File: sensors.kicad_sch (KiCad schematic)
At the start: 13 parts, among them U3 BMP581, U4 BNO085, Y2 Crystal

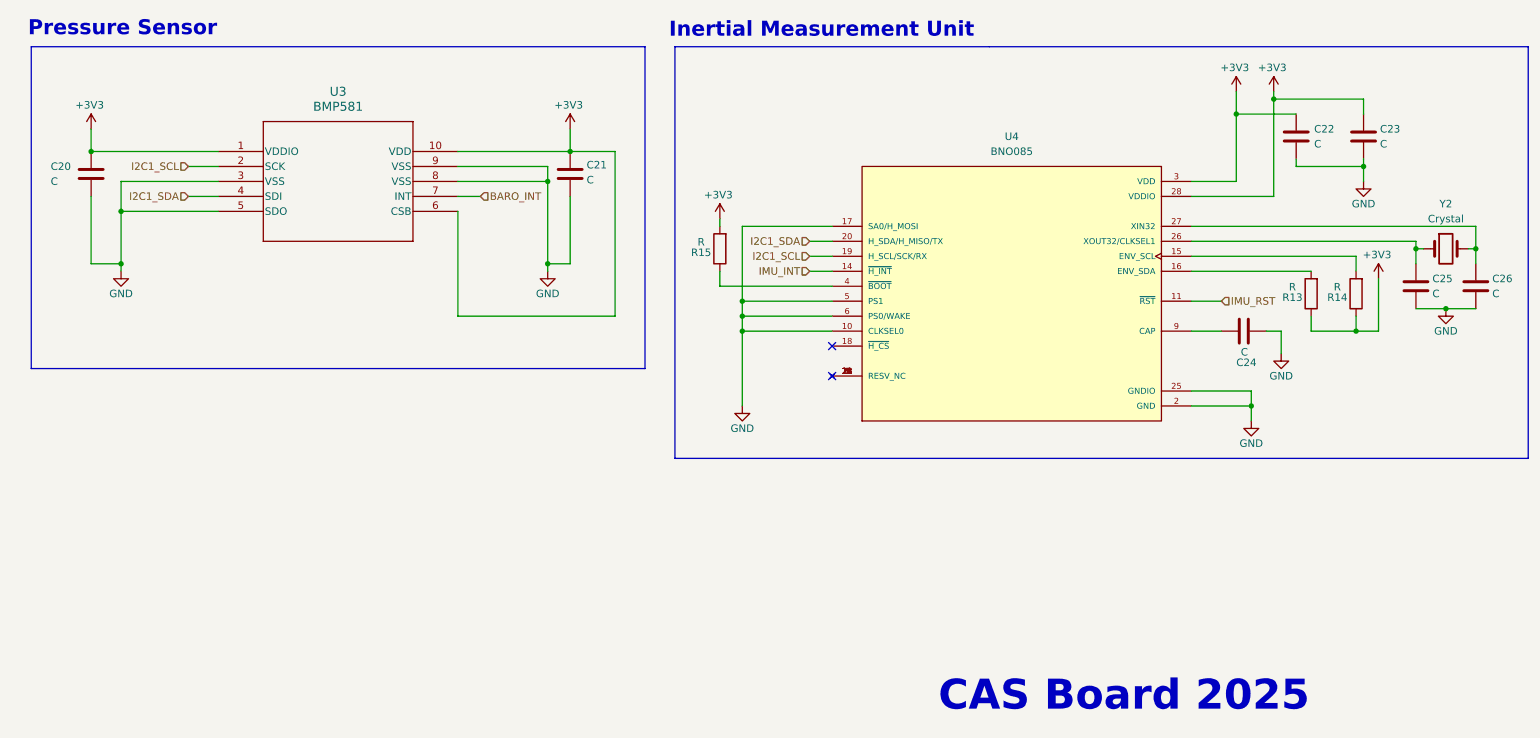
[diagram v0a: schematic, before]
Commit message: Initial layout for PCB components, updated README with images. Removed some test points and headers from final layout. Pending addition of buzzer. Pending additional power testing and pending routing.
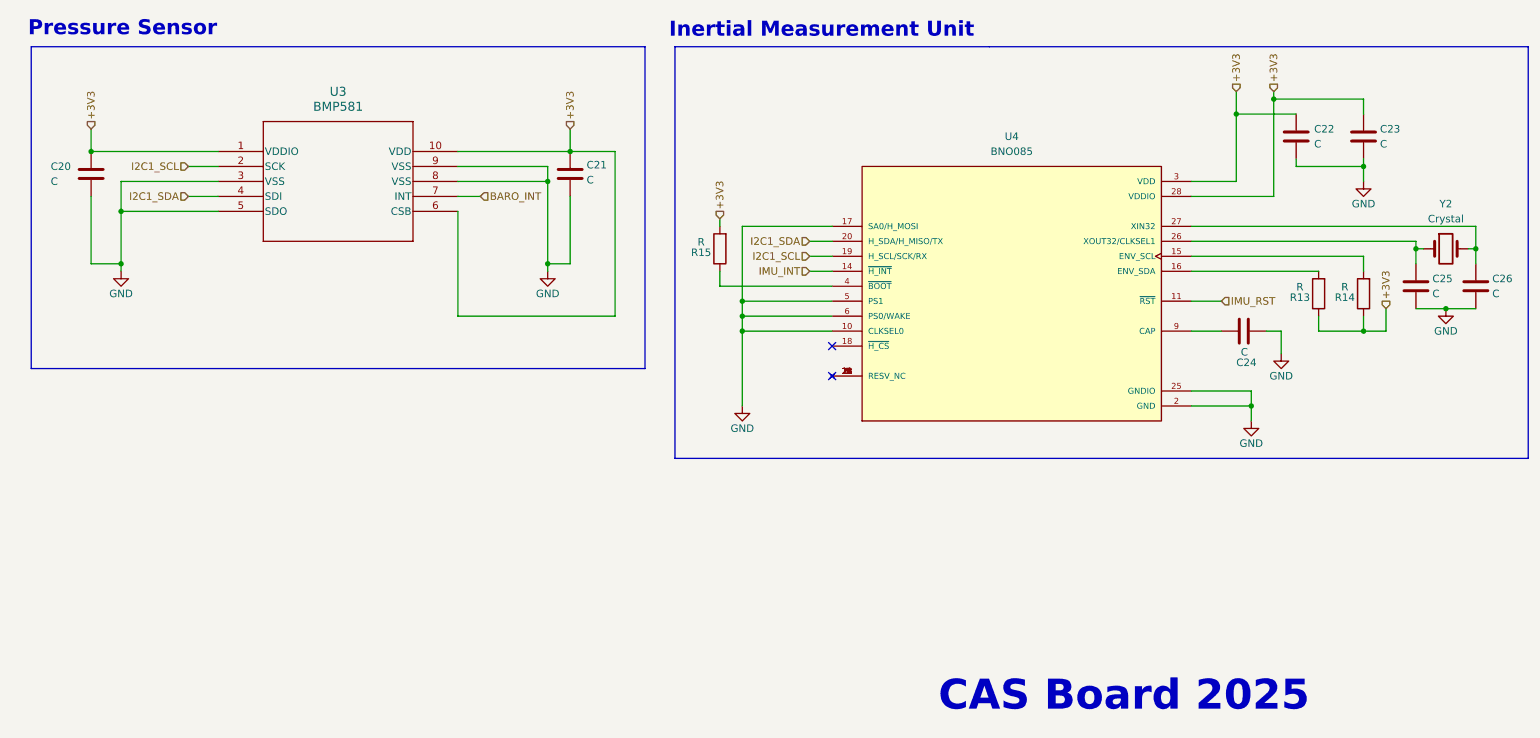
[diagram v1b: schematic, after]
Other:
- moved on the sheet: R13, R14

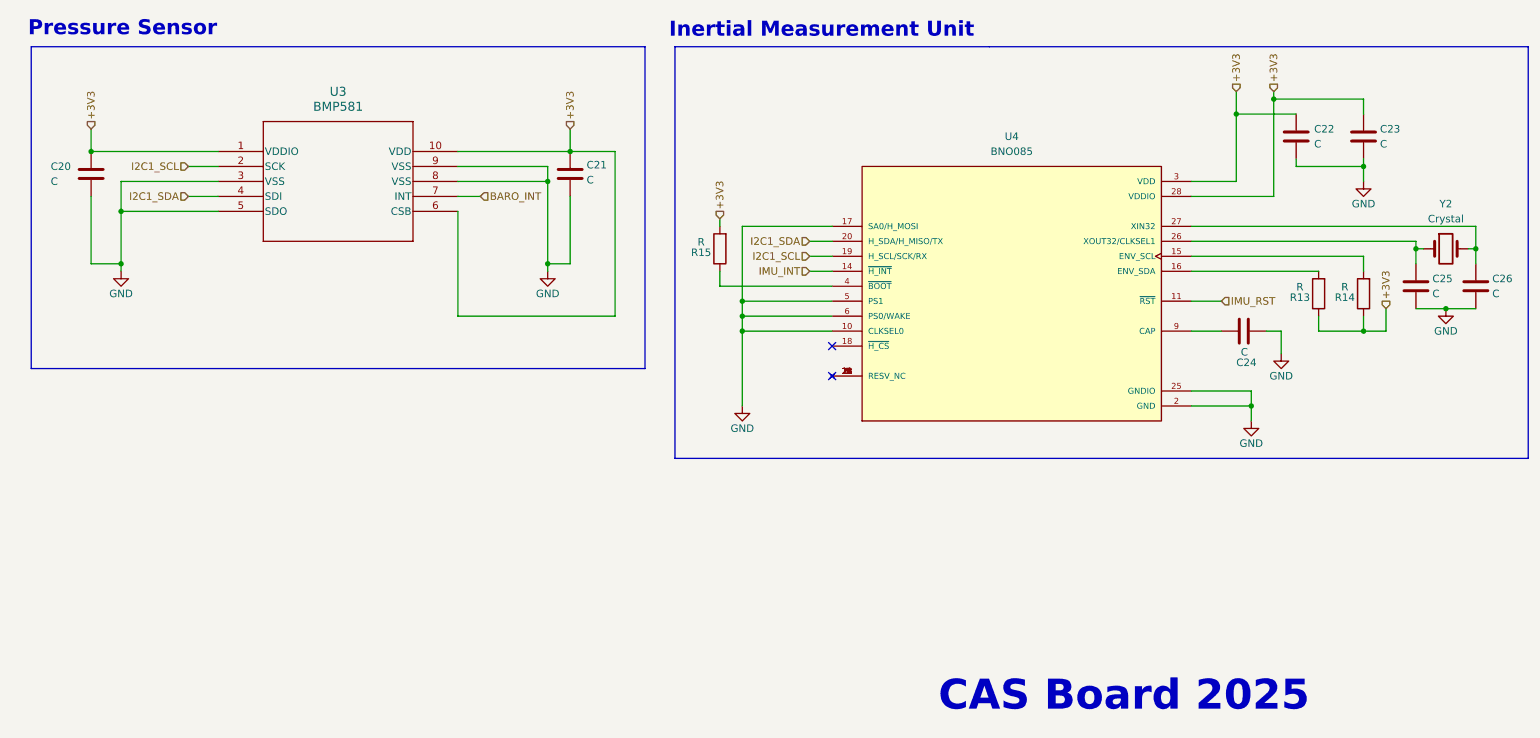
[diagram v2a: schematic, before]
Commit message: Removed uncvessary test points and headerrs. Added missing values. Update images of schematics
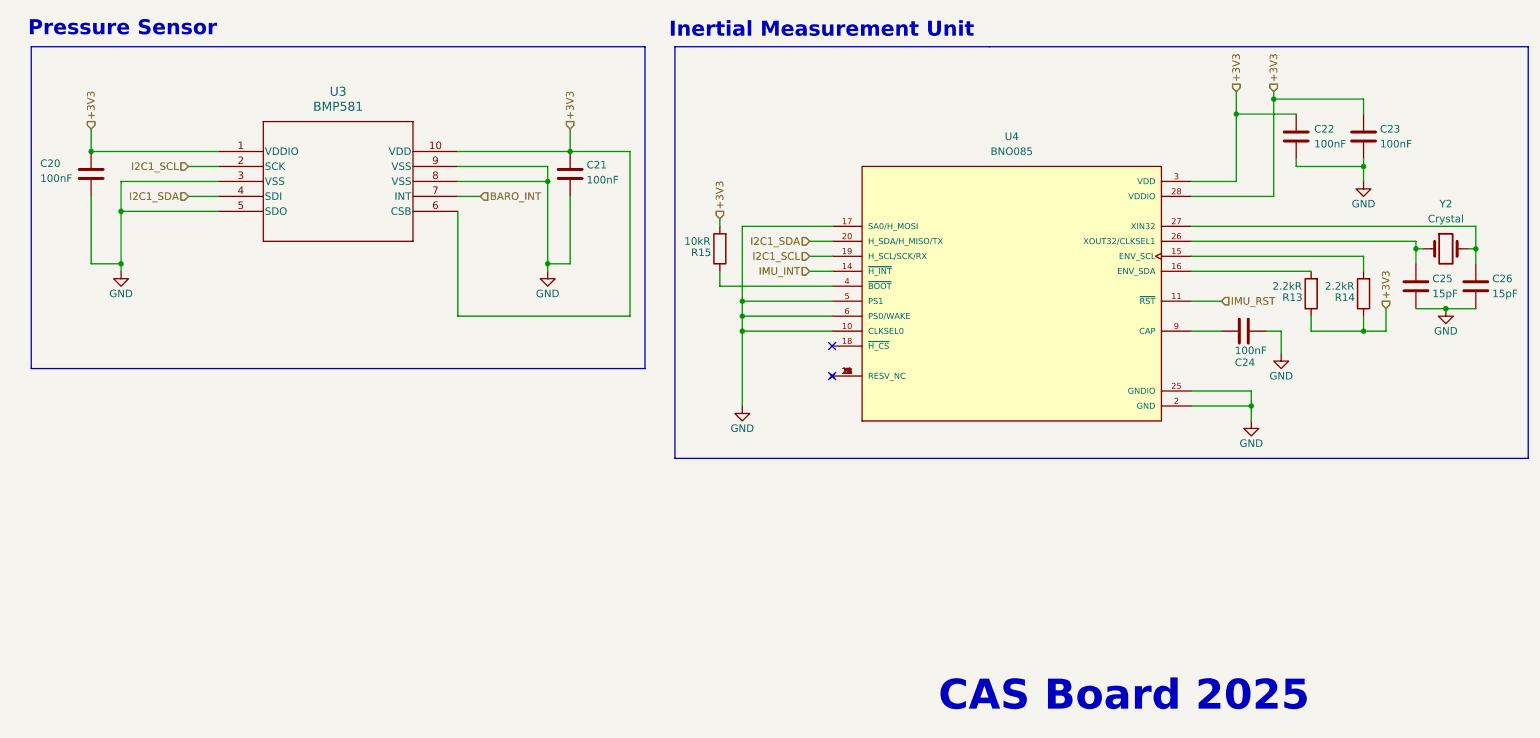
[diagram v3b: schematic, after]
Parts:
- C20, C21, C22, C23, C24: value C -> 100nF
- C25, C26: value C -> 15pF
- R13, R14: value R -> 2.2kR
- R15: value R -> 10kR
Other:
- moved on the sheet: R13
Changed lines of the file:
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@@
 	(wire
 		(pts
-			(xy 220.98 101.6) (xy 242.57 101.6)
+			(xy 220.98 101.6) (xy 241.3 101.6)
 		)
 		(stroke
@@
 	(wire
 		(pts
-			(xy 242.57 109.22) (xy 242.57 111.76)
+			(xy 241.3 109.22) (xy 241.3 111.76)
 		)
 		(stroke
@@
 	(wire
 		(pts
-			(xy 96.52 109.22) (xy 123.19 109.22)
+			(xy 96.52 109.22) (xy 125.73 109.22)
 		)
 		(stroke
@@
 	(wire
 		(pts
-			(xy 123.19 81.28) (xy 115.57 81.28)
+			(xy 125.73 81.28) (xy 115.57 81.28)
 		)
 		(stroke
@@
 	(wire
 		(pts
-			(xy 123.19 109.22) (xy 123.19 81.28)
+			(xy 125.73 109.22) (xy 125.73 81.28)
 		)
 		(stroke
@@
 	(wire
 		(pts
-			(xy 242.57 111.76) (xy 250.19 111.76)
+			(xy 241.3 111.76) (xy 250.19 111.76)
 		)
 		(stroke
@@
 			)
 		)
-		(property "Value" "C"
+		(property "Value" "100nF"
 			(at 252.984 80.01 0)
 			(effects
@@
 			)
 		)
-		(property "Value" "C"
+		(property "Value" "15pF"
 			(at 261.874 105.41 0)
 			(effects
@@
 			)
 		)
-		(property "Value" "C"
+		(property "Value" "100nF"
 			(at 241.808 80.01 0)
 			(effects
@@
 	(symbol
 		(lib_id "Device:R")
-		(at 242.57 105.41 180)
+		(at 241.3 105.41 180)
 		(unit 1)
 		(exclude_from_sim no)
@@
 		(dnp no)
 		(property "Reference" "R13"
-			(at 239.395 106.045 0)
+			(at 238.125 106.045 0)
 			(effects
 				(font
@@
 			)
 		)
-		(property "Value" "R"
-			(at 239.395 104.267 0)
+		(property "Value" "2.2kR"
+			(at 237.236 104.14 0)
 			(effects
 				(font
@@
 		)
 		(property "Footprint" "Resistor_SMD:R_0805_2012Metric_Pad1.20x1.40mm_HandSolder"
-			(at 244.348 105.41 90)
+			(at 243.078 105.41 90)
 			(effects
 				(font
@@
 		)
 		(property "Datasheet" "~"
-			(at 242.57 105.41 0)
+			(at 241.3 105.41 0)
 			(effects
 				(font
@@
 		)
 		(property "Description" "Resistor"
-			(at 242.57 105.41 0)
+			(at 241.3 105.41 0)
 			(effects
 				(font
@@
 			)
 		)
-		(property "Value" "R"
-			(at 247.015 104.267 0)
+		(property "Value" "2.2kR"
+			(at 246.126 104.14 0)
 			(effects
 				(font
@@
 			)
 		)
-		(property "Value" "C"
+		(property "Value" "100nF"
 			(at 118.364 86.106 0)
 			(effects
@@
 		(dnp no)
 		(property "Reference" "C20"
-			(at 27.432 83.82 0)
+			(at 25.654 83.312 0)
 			(effects
 				(font
@@
 			)
 		)
-		(property "Value" "C"
-			(at 27.432 86.36 0)
+		(property "Value" "100nF"
+			(at 25.654 85.852 0)
 			(effects
 				(font
@@
 			)
 		)
-		(property "Value" "C"
+		(property "Value" "15pF"
 			(at 272.034 105.41 0)
 			(effects
@@
 		(dnp no)
 		(property "Reference" "C24"
-			(at 228.6 117.094 90)
+			(at 228.346 117.094 90)
 			(effects
 				(font
@@
 			)
 		)
-		(property "Value" "C"
-			(at 229.362 115.316 90)
+		(property "Value" "100nF"
+			(at 228.346 115.062 90)
 			(effects
 				(font
@@
 			)
 		)
-		(property "Value" "R"
-			(at 137.795 96.647 0)
+		(property "Value" "10kR"
+			(at 137.16 96.52 0)
 			(effects
 				(font

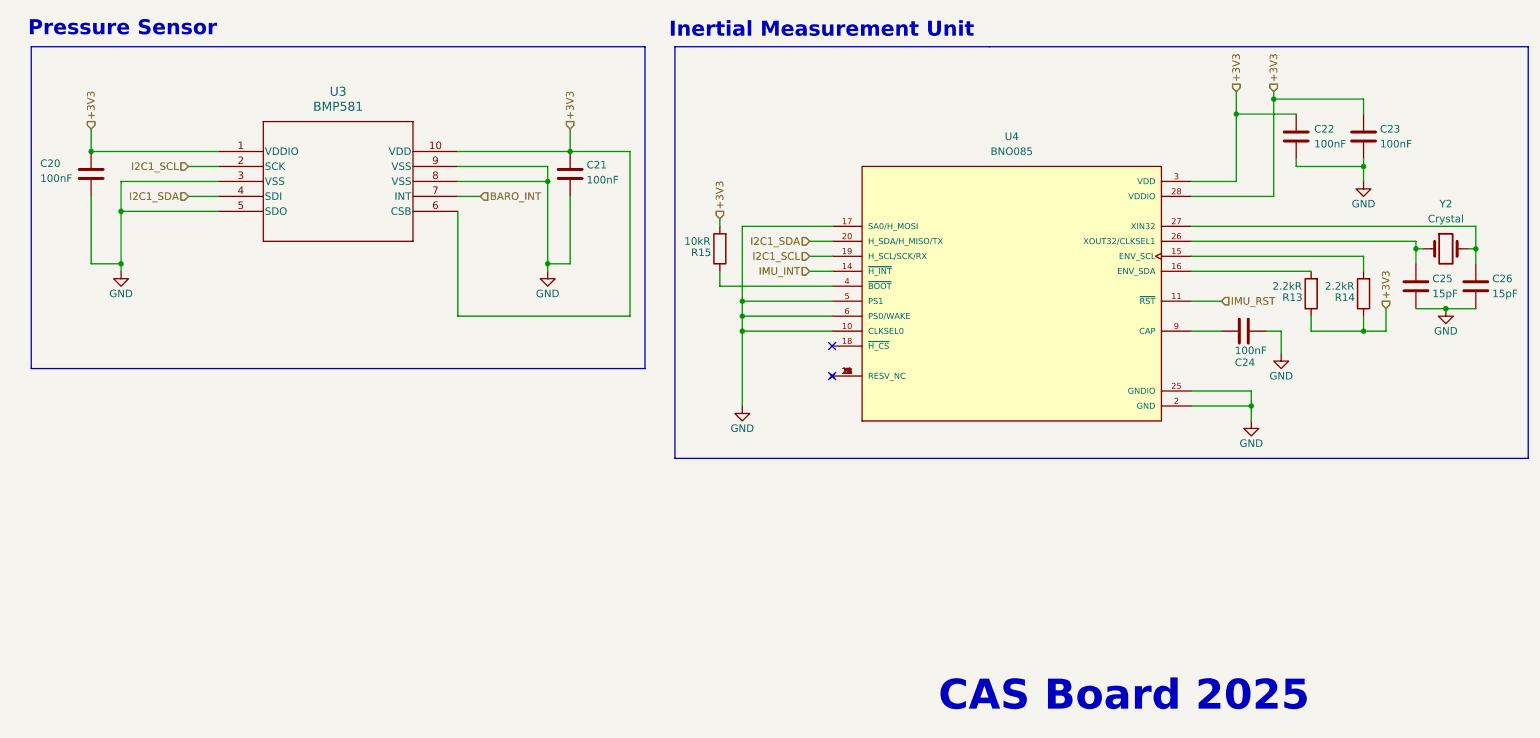
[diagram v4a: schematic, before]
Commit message: Adi made some fixes to schematic
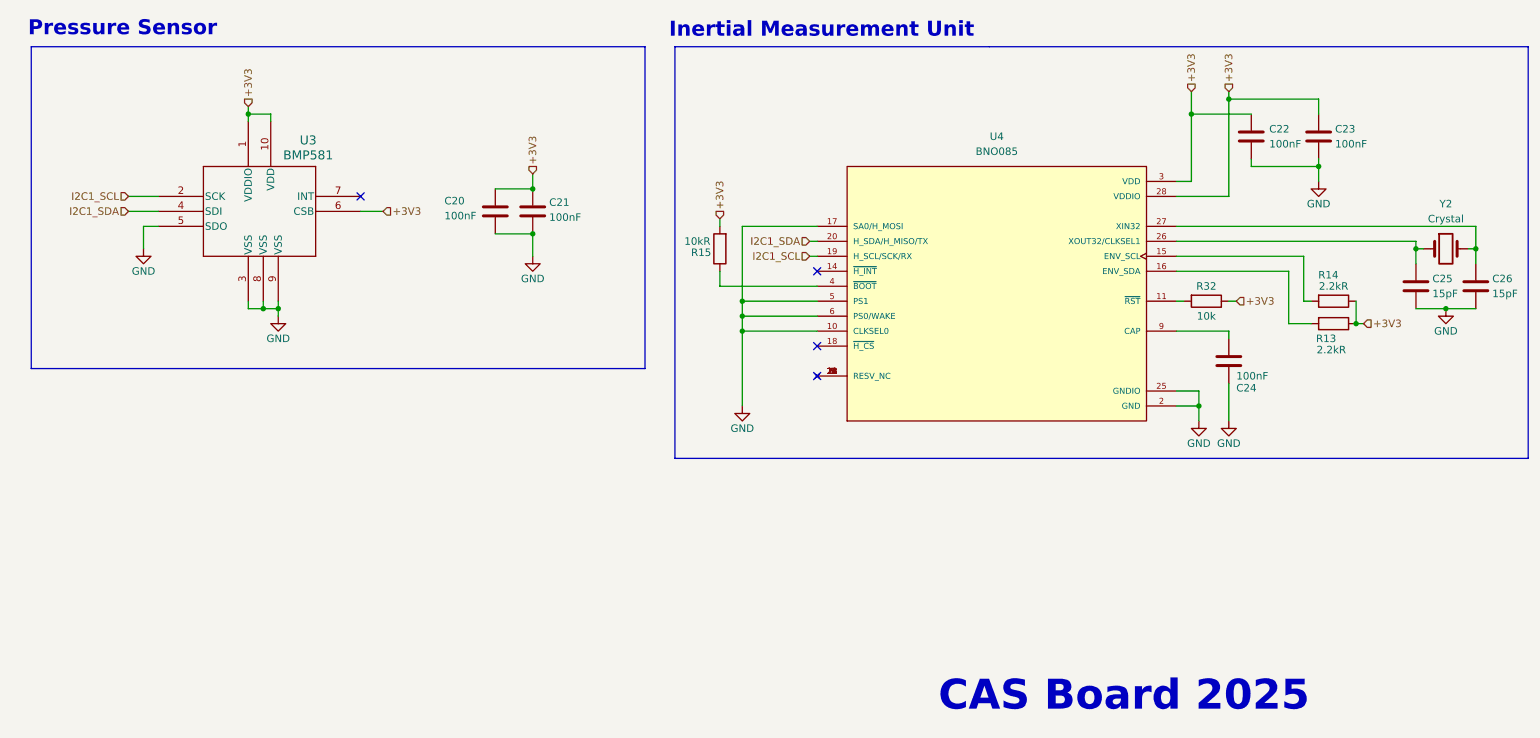
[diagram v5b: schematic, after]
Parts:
- added R32: 10k, Resistor_SMD:R_0805_2012Metric_Pad1.20x1.40mm_HandSolder, symbol Device:R
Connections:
- net +3V3: now also R32.1
- net BARO_INT: no longer names the net of U3.7 (INT)
- net IMU_INT: no longer names the net of U4.14 (~{H_INT})
- net IMU_RST: no longer names the net of U4.11 (~{RST})
- net IMU_RST: now also R32.2
- no-connect marks 2 -> 4
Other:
- moved on the sheet: C20, C21, C22, C23, C24, R13, R14, U3, U4
